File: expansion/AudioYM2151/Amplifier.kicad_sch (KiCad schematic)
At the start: 21 parts, among them J3 Audio Out, U7 TPA3122D2

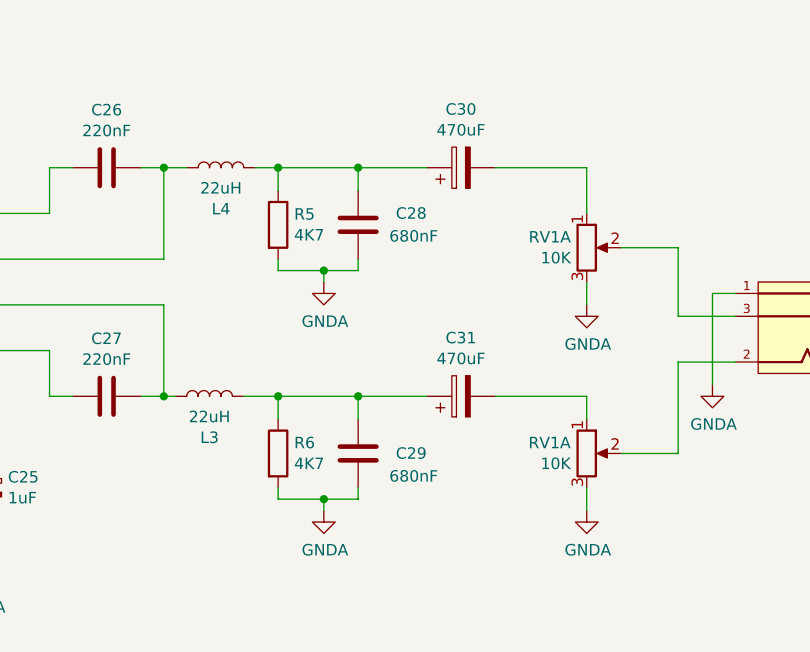
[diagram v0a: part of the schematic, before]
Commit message: All projects updated to KiCAD 7 format files
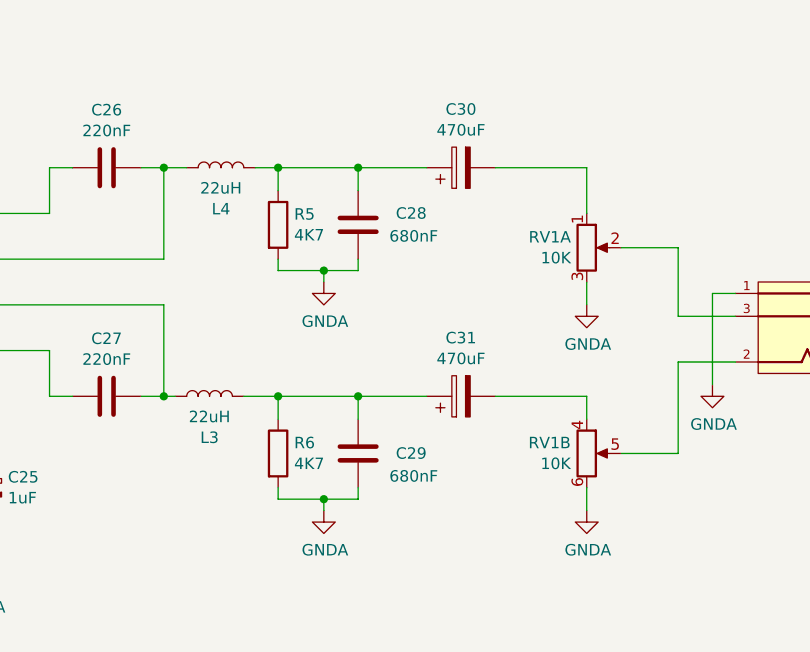
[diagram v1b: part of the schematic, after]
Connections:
- net GNDA: now also RV1.6; no longer RV1.3
- net at C31.2: now also RV1.4; no longer RV1.1
- net at J3.2: now also RV1.5; no longer RV1.2

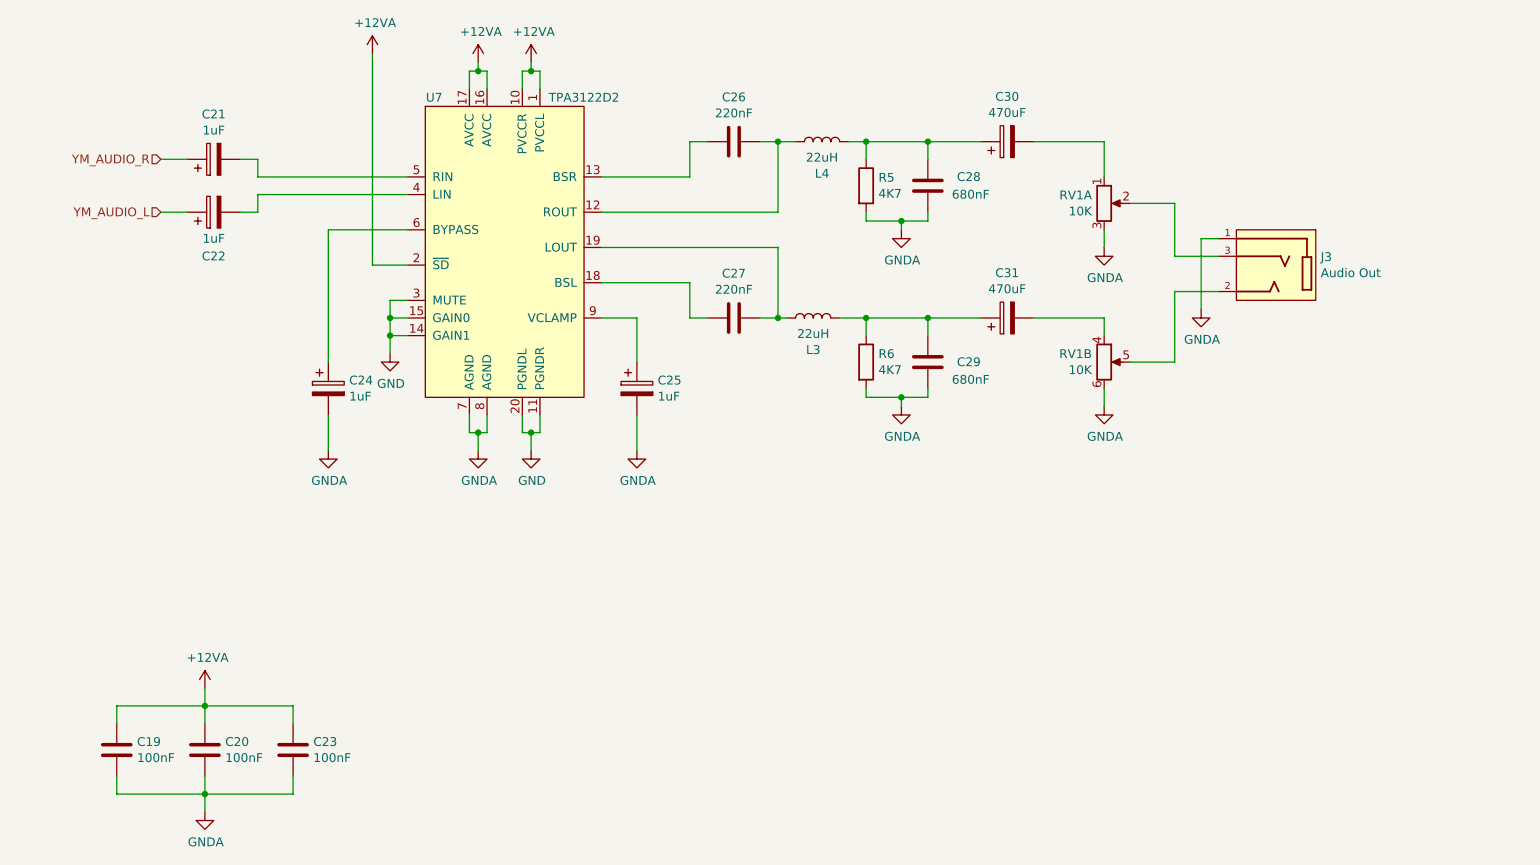
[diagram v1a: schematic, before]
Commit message: Modified volume control on YM2151 card
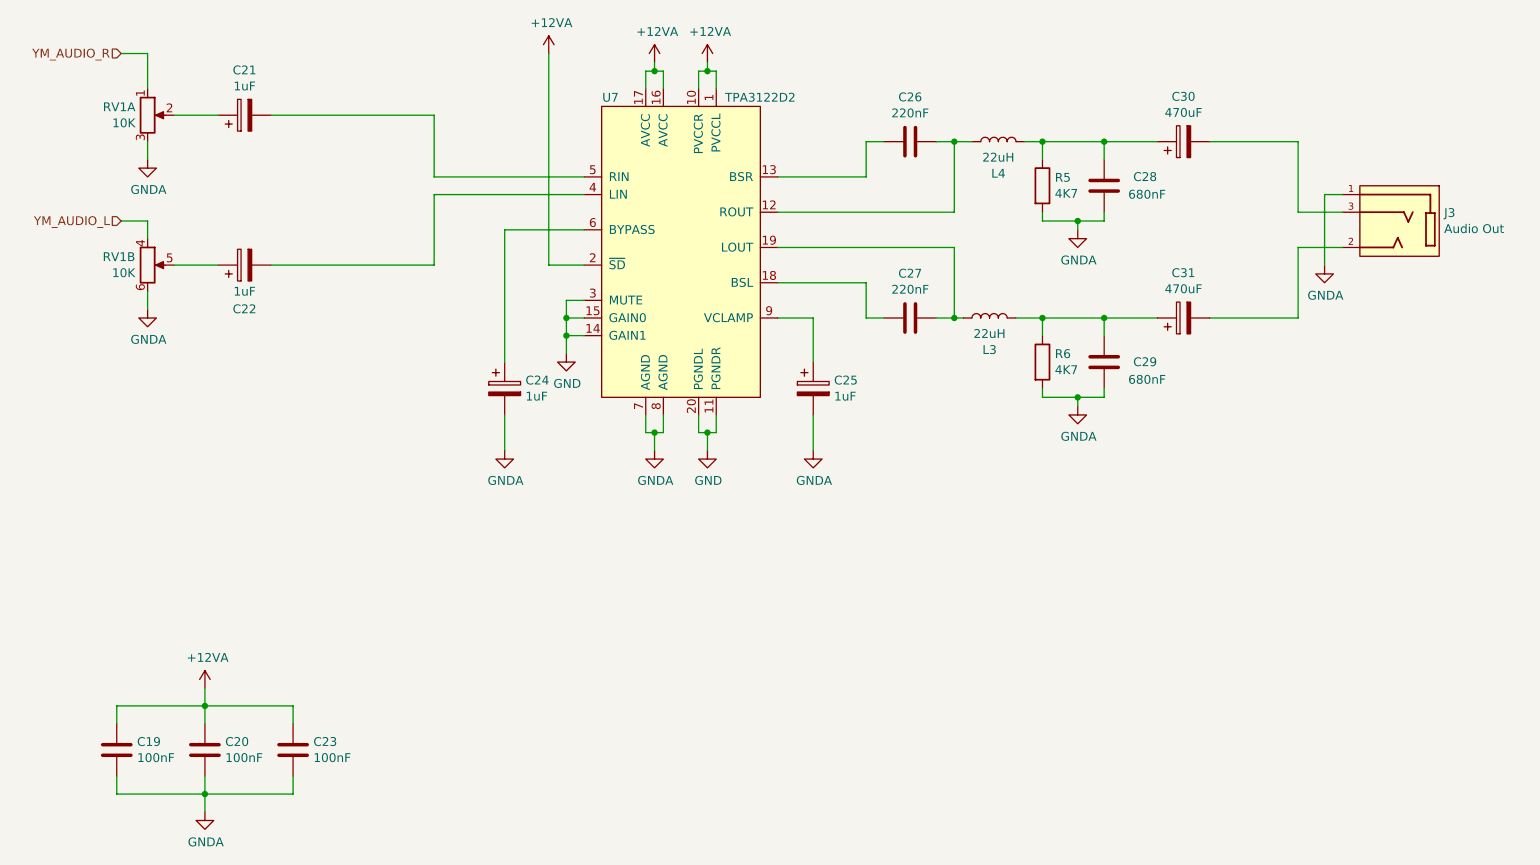
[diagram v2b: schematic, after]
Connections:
- net YM_AUDIO_L: now also RV1.4; no longer C22.1
- net YM_AUDIO_R: now also RV1.1; no longer C21.1
- net at C30.2: now also J3.3; no longer RV1.1
- net at C31.2: now also J3.2; no longer RV1.4
- net at RV1.2: now also C21.1; no longer J3.3
- net at RV1.5: now also C22.1; no longer J3.2
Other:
- moved on the sheet: C21, C22, C24, C25, C26, C27, C28, C29, C30, C31, J3, L3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
